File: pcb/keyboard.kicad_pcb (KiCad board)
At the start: 4 copper layers, 304.8 x 119.1 mm, 197 parts, among them J1 Conn_ARM_JTAG_SWD_10, J2 USB_C_Receptacle_USB2.0_16P, J3 Conn_Coaxial, K1 KEYSW, K10 KEYSW, K11 KEYSW, K12 KEYSW, K13 KEYSW, K14 KEYSW, K15 KEYSW, K16 KEYSW, K17 KEYSW, K18 KEYSW, K19 KEYSW, K2 KEYSW, K20 KEYSW, K21 KEYSW, K22 KEYSW, K23 KEYSW, K24 KEYSW, K25 KEYSW, K26 KEYSW, K27 KEYSW, K28 KEYSW, K29 KEYSW, K3 KEYSW, K30 KEYSW, K31 KEYSW, K32 KEYSW, K33 KEYSW, K34 KEYSW, K35 KEYSW, K36 KEYSW, K37 KEYSW, K38 KEYSW, K39 KEYSW, K4 KEYSW, K40 KEYSW, K41 KEYSW, K42 KEYSW, K43 KEYSW, K45 KEYSW, K46 KEYSW, K47 KEYSW, K48 KEYSW, K49 KEYSW, K5 KEYSW, K50 KEYSW, K51 KEYSW, K52 KEYSW, K53 KEYSW, K54 KEYSW, K55 KEYSW, K56 KEYSW, K57 KEYSW, K58 KEYSW, K59 KEYSW, K6 KEYSW, K60 KEYSW, K61 KEYSW, K62 KEYSW, K63 KEYSW, K67 KEYSW, K7 KEYSW, K70 KEYSW, K71 KEYSW, K72 KEYSW, K73 KEYSW, K74 KEYSW, K75 KEYSW, K8 KEYSW, K9 KEYSW, Q1 FDN340P, Q2 FS8025A, Q3 FDN340P, SW1 SW_SPST, SW2 SW_SPST, U1 nRF52840, U2 TP4056-42-ESOP8, U3 DW01A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

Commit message: Improve clock placement and round corners
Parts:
- moved C10 6.95 mm to (243.2, 86.3)
- moved C12 5.83 mm to (235.5, 81.0), turned to 90 degrees
- moved C2 3.64 mm to (242.0, 84.8), turned to 180 degrees
- moved L3 2.84 mm to (227.0, 80.0), turned to 180 degrees
- moved L2 2.09 mm to (227.0, 82.0), turned to 0 degrees
- moved X1 2.02 mm to (238.9, 83.0), turned to -45 degrees
- moved C1 1.81 mm to (237.0, 80.0)
- moved C13 1.35 mm to (234.0, 81.0)
- moved C16 1.11 mm to (231.0, 80.0)
- moved C15 1.09 mm to (231.0, 82.0)
- moved C9 0.22 mm to (239.8, 86.4)
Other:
- outline, holes or cut-outs redrawn

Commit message: Move some parts around lol
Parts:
- moved R3 83.9 mm to (115.0, 93.0), turned to 0 degrees
- moved F1 72.7 mm to (115.0, 87.0), turned to 90 degrees
- moved D64 61.1 mm to (107.0, 93.0), turned to 0 degrees
- moved C11 57.2 mm to (153.7, 94.0)
- moved Q2 52.4 mm to (151.0, 86.0)
- moved U3 51.2 mm to (141.0, 86.0)
- moved R6 45.5 mm to (137.0, 81.0), turned to 0 degrees
- moved D68 44.1 mm to (130.0, 84.0), turned to 90 degrees
- moved R8 40.9 mm to (133.0, 86.0), turned to 0 degrees
- moved R9 37.3 mm to (146.0, 86.0), turned to 0 degrees
- moved R11 28.5 mm to (132.0, 80.0), turned to -90 degrees
- moved C17 28.3 mm to (137.0, 85.0), turned to 90 degrees
- moved C18 24.3 mm to (141.0, 82.0), turned to -90 degrees
- moved Q1 21.7 mm to (119.0, 84.0)
- moved Q3 19.7 mm to (125.5, 84.0)
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
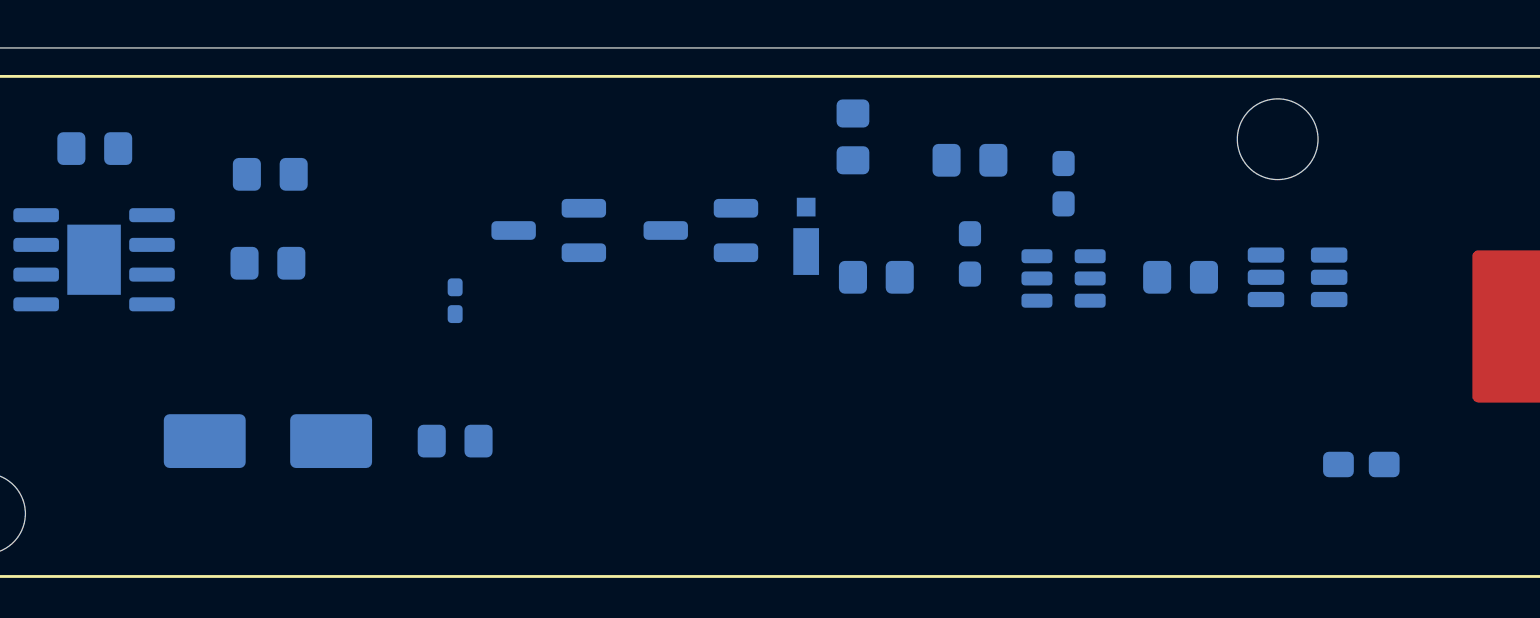
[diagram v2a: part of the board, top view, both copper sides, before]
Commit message: Finish initial placement
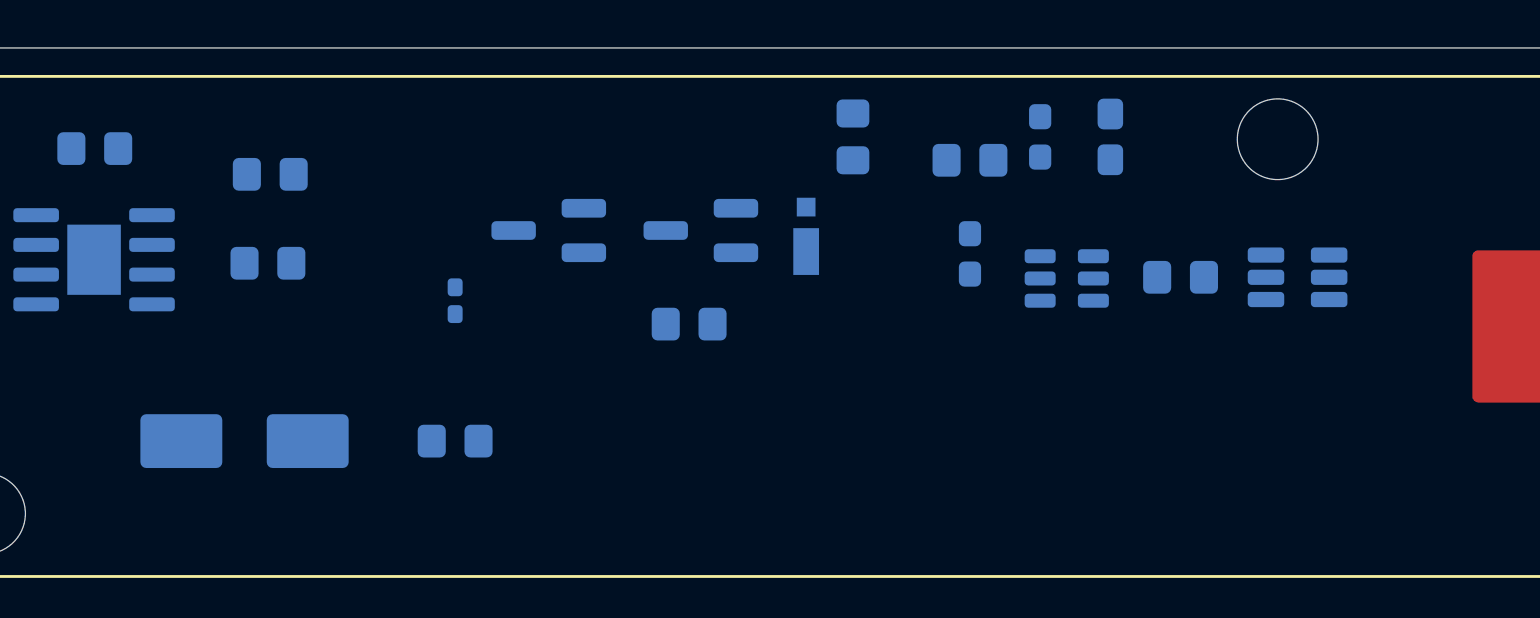
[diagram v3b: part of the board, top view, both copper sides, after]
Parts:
- moved C11 17.6 mm to (143.0, 80.0), turned to 90 degrees
- moved R8 8.25 mm to (125.0, 88.0)
- moved C18 2.24 mm to (140.0, 80.0), turned to 90 degrees
- moved D64 1.00 mm to (106.0, 93.0)
- moved U3 0.14 mm to (141.1, 86.0)
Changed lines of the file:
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@@
 		(tags "resistor handsolder")
 		(property "Reference" "R6"
-			(at 0 1.65 0)
+			(at 0 -1.6 0)
 			(layer "B.SilkS")
 			(effects
@@
 	(footprint "Diode_SMD:D_SMB_Handsoldering"
 		(layer "B.Cu")
-		(at 107 93)
+		(at 106 93)
 		(descr "Diode SMB (DO-214AA) Handsoldering")
 		(tags "Diode SMB (DO-214AA) Handsoldering")
@@
 	(footprint "Resistor_SMD:R_0805_2012Metric_Pad1.20x1.40mm_HandSolder"
 		(layer "B.Cu")
-		(at 133 86)
+		(at 125 88)
 		(descr "Resistor SMD 0805 (2012 Metric), square (rectangular) end terminal, IPC-7351 nominal with elongated pad for handsoldering. (Body size source: IPC-SM-782 page 72, https://www.pcb-3d.com/wordpress/wp-content/uploads/ipc-sm-782a_amendment_1_and_2.pdf)")
 		(tags "resistor handsolder")
@@
 	(footprint "Package_TO_SOT_SMD:SOT-23-6"
 		(layer "B.Cu")
-		(at 141 86.05 180)
+		(at 141.1375 86.05 180)
 		(descr "SOT, 6 Pin (JEDEC MO-178 Var AB https://www.jedec.org/document_search?search_api_views_fulltext=MO-178)")
 		(tags "SOT TO_SOT_SMD")
@@
 	(footprint "Capacitor_Tantalum_SMD:CP_EIA-2012-15_AVX-P_HandSolder"
 		(layer "B.Cu")
-		(at 153.725 94 180)
+		(at 143 80 90)
 		(descr "Tantalum Capacitor SMD AVX-P (2012-15 Metric), IPC-7352 nominal, (Body size from: https://www.vishay.com/docs/40182/tmch.pdf)")
 		(tags "capacitor tantalum")
 		(property "Reference" "C11"
-			(at 0 1.58 0)
+			(at 0 1.58 90)
 			(layer "B.SilkS")
 			(effects
@@
 		)
 		(property "Value" "10µF"
-			(at 0 -1.58 0)
+			(at 0 -1.58 90)
 			(layer "B.Fab")
 			(hide yes)
@@
 		)
 		(property "Datasheet" ""
-			(at 0 0 0)
+			(at 0 0 90)
 			(layer "B.Fab")
 			(hide yes)
@@
 		)
 		(property "Description" "Polarized capacitor"
-			(at 0 0 0)
+			(at 0 0 90)
 			(layer "B.Fab")
 			(hide yes)
@@
 		)
 		(property "KiLib_Generator" "SMD_2terminal_chip_molded"
-			(at 0 0 0)
+			(at 0 0 90)
 			(layer "B.SilkS")
 			(hide yes)
@@
 		(duplicate_pad_numbers_are_jumpers no)
 		(fp_line
-			(start 1 0.805)
-			(end -1.895 0.805)
+			(start -1.895 -0.805)
+			(end 1 -0.805)
 			(stroke
 				(width 0.12)
@@
 		)
 		(fp_line
-			(start -1.895 0.805)
-			(end -1.895 -0.805)
+			(start 1 0.805)
+			(end -1.895 0.805)
 			(stroke
 				(width 0.12)
@@
 		)
 		(fp_line
-			(start -1.895 -0.805)
-			(end 1 -0.805)
+			(start -1.895 0.805)
+			(end -1.895 -0.805)
 			(stroke
 				(width 0.12)
@@
 		)
 		(fp_line
-			(start 1 0.625)
-			(end -0.6875 0.625)
+			(start 1 -0.625)
+			(end 1 0.625)
 			(stroke
 				(width 0.1)
@@
 		)
 		(fp_line
-			(start 1 -0.625)
-			(end 1 0.625)
+			(start -1 -0.625)
+			(end 1 -0.625)
 			(stroke
 				(width 0.1)
@@
 		)
 		(fp_line
-			(start -0.6875 0.625)
-			(end -1 0.3125)
+			(start -1 0.3125)
+			(end -1 -0.625)
 			(stroke
 				(width 0.1)
@@
 		)
 		(fp_line
-			(start -1 0.3125)
-			(end -1 -0.625)
+			(start 1 0.625)
+			(end -0.6875 0.625)
 			(stroke
 				(width 0.1)
@@
 		)
 		(fp_line
-			(start -1 -0.625)
-			(end 1 -0.625)
+			(start -0.6875 0.625)
+			(end -1 0.3125)
 			(stroke
 				(width 0.1)
@@
 		)
 		(fp_text user "${REFERENCE}"
-			(at 0 0 0)
+			(at 0 0 90)
 			(layer "B.Fab")
 			(effects
@@
 		)
 		(pad "1" smd roundrect
-			(at -0.9775 0 180)
+			(at -0.9775 0 90)
 			(size 1.315 1.09)
 			(layers "B.Cu" "B.Mask" "B.Paste")
@@
 		)
 		(pad "2" smd roundrect
-			(at 0.9775 0 180)
+			(at 0.9775 0 90)
 			(size 1.315 1.09)
 			(layers "B.Cu" "B.Mask" "B.Paste")
@@
 	(footprint "Capacitor_SMD:C_0603_1608Metric_Pad1.08x0.95mm_HandSolder"
 		(layer "B.Cu")
-		(at 141 82 -90)
+		(at 140 80 90)
 		(descr "Capacitor SMD 0603 (1608 Metric), square (rectangular) end terminal, IPC-7351 nominal with elongated pad for handsoldering. (Body size source: IPC-SM-782 page 76, https://www.pcb-3d.com/wordpress/wp-content/uploads/ipc-sm-782a_amendment_1_and_2.pdf)")
 		(tags "capacitor handsolder")
@@
 		(duplicate_pad_numbers_are_jumpers no)
 		(fp_line
-			(start -0.146267 0.51)
-			(end 0.146267 0.51)
+			(start -0.146267 -0.51)
+			(end 0.146267 -0.51)
 			(stroke
 				(width 0.12)
@@
 		)
 		(fp_line
-			(start -0.146267 -0.51)
-			(end 0.146267 -0.51)
+			(start -0.146267 0.51)
+			(end 0.146267 0.51)
 			(stroke
 				(width 0.12)
@@
 		)
 		(pad "1" smd roundrect
-			(at -0.8625 0 270)
+			(at -0.8625 0 90)
 			(size 1.075 0.95)
 			(layers "B.Cu" "B.Mask" "B.Paste")
@@
 		)
 		(pad "2" smd roundrect
-			(at 0.8625 0 270)
+			(at 0.8625 0 90)
 			(size 1.075 0.95)
 			(layers "B.Cu" "B.Mask" "B.Paste")

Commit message: Add mounting points
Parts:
- added H1: MountingHole_Pad, MountingHole:MountingHole_2.2mm_M2_Pad_Via, F.Cu at (55.0, 85.0)
- added H2: MountingHole_Pad, MountingHole:MountingHole_2.2mm_M2_Pad_Via, F.Cu at (250.0, 81.2)
- added H3: MountingHole_Pad, MountingHole:MountingHole_2.2mm_M2_Pad_Via, F.Cu at (332.0, 121.0)
- added H4: MountingHole_Pad, MountingHole:MountingHole_2.2mm_M2_Pad_Via, F.Cu at (140.0, 186.0)
- added H5: MountingHole_Pad, MountingHole:MountingHole_2.2mm_M2_Pad_Via, F.Cu at (164.8, 81.0)
- added H6: MountingHole_Pad, MountingHole:MountingHole_2.2mm_M2_Pad_Via, F.Cu at (71.0, 184.0)
- added H7: MountingHole_Pad, MountingHole:MountingHole_2.2mm_M2_Pad_Via, F.Cu at (235.0, 184.8)
- added H8: MountingHole_Pad, MountingHole:MountingHole_2.2mm_M2_Pad_Via, F.Cu at (310.0, 175.0)
- added H9: MountingHole_Pad, MountingHole:MountingHole_2.2mm_M2_Pad_Via, F.Cu at (195.0, 139.0)

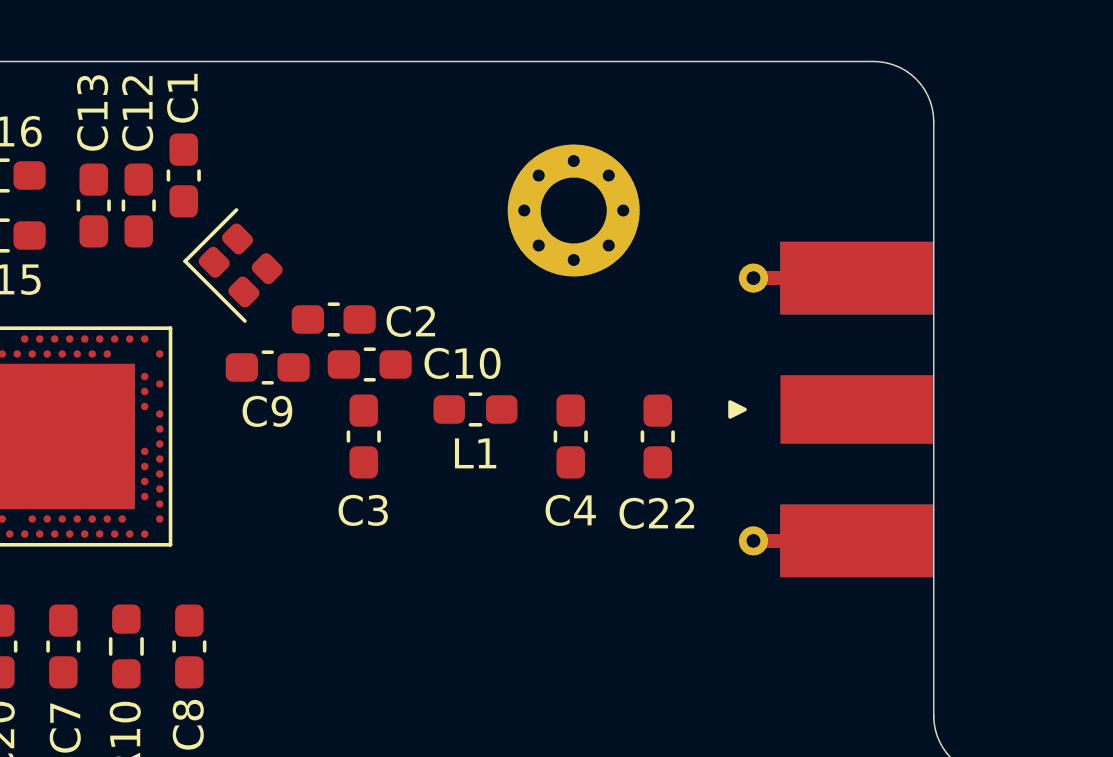
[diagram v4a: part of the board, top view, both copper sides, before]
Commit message: Add final hand solder footprints
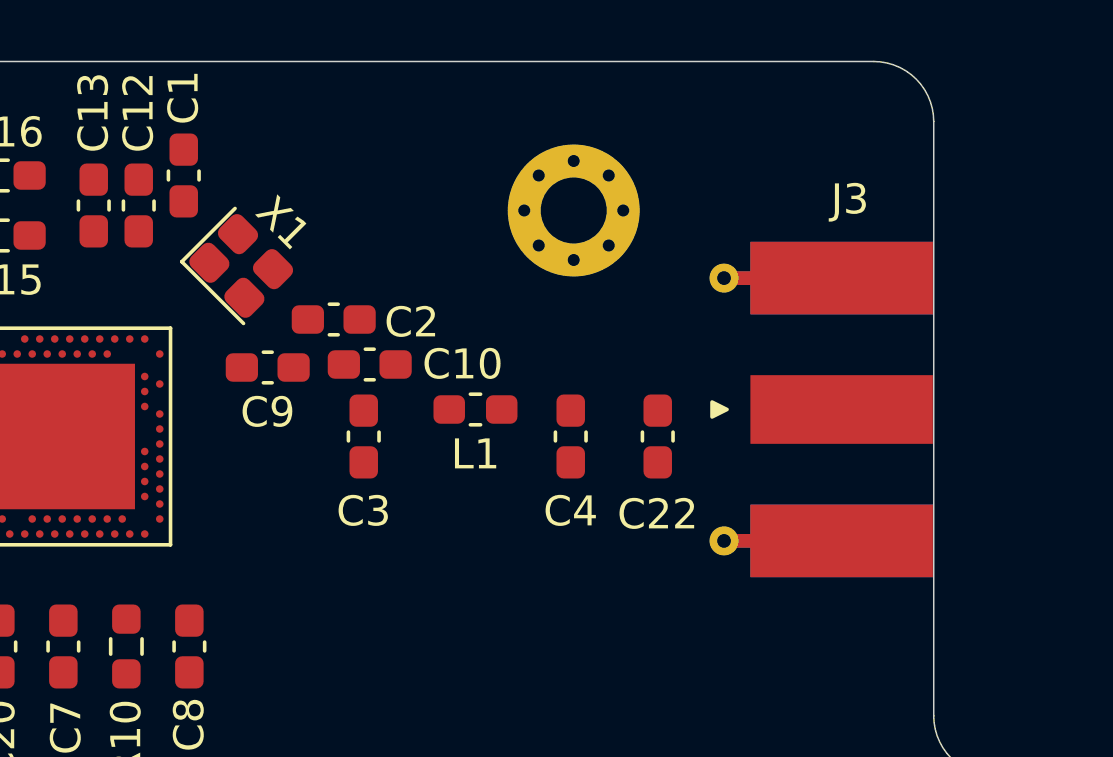
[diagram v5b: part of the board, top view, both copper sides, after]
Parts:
- J3: footprint Connector_Coaxial:SMA_Molex_73251-1153_EdgeMount_Horizontal -> My_Footprints:SMA_Molex_73251-1153_EdgeMount_Horizontal_HandSolder
- X1: footprint Crystal:Crystal_SMD_2016-4Pin_2.0x1.6mm -> My_Footprints:Crystal_SMD_2016-4Pin_2.0x1.6mm_HandSolder
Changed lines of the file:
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@@
 		(embedded_fonts no)
 	)
-	(footprint "Crystal:Crystal_SMD_2016-4Pin_2.0x1.6mm"
+	(footprint "My_Footprints:Crystal_SMD_2016-4Pin_2.0x1.6mm_HandSolder"
 		(layer "F.Cu")
 		(at 238.9 83 -45)
 		(descr "SMD2016/4, Crystal, 2.0x1.6mm package, SMD, http://www.q-crystal.com/upload/5/2015552223166229.pdf")
 		(property "Reference" "X1"
-			(at 0.000001 2.199999 135)
+			(at 0 -2.000001 315)
 			(layer "F.SilkS")
-			(hide yes)
 			(effects
 				(font
@@
 		)
 		(property "Value" "32MHz"
-			(at 0 2.000001 135)
+			(at 0 2.000001 315)
 			(layer "F.Fab")
 			(hide yes)
@@
 		)
 		(property "Datasheet" ""
-			(at 0 0 135)
+			(at 0 0 315)
 			(layer "F.Fab")
 			(hide yes)
@@
 		)
 		(property "Description" ""
-			(at 0 0 135)
+			(at 0 0 315)
 			(layer "F.Fab")
 			(hide yes)
@@
 		)
 		(property "KiLib_Generator" "crystal_resonator_oscillator"
-			(at 0 0 135)
+			(at 0 0 315)
 			(layer "F.SilkS")
 			(hide yes)
@@
 		(duplicate_pad_numbers_are_jumpers no)
 		(fp_line
-			(start -1.41 1.21)
-			(end 1.41 1.21)
+			(start -1.478319 1.3)
+			(end 1.431681 1.3)
 			(stroke
 				(width 0.12)
@@
 		)
 		(fp_line
-			(start -1.41 -1.21)
-			(end -1.41 1.21)
+			(start -1.478319 -1.21)
+			(end -1.478319 1.3)
 			(stroke
 				(width 0.12)
@@
 		(fp_poly
 			(pts
-				(xy -1.5 -1.3) (xy 1.5 -1.3) (xy 1.5 1.3) (xy -1.5 1.3)
+				(xy -1.578319 -1.3) (xy 1.521681 -1.3) (xy 1.52168 1.4) (xy -1.57832 1.4)
 			)
 			(stroke
@@
 		(fp_poly
 			(pts
-				(xy 1 -0.800001) (xy 1 0.8) (xy -0.6 0.799999) (xy -1 0.4) (xy -1 -0.8)
+				(xy 1.021681 -0.8) (xy 1.021681 0.8) (xy -0.578319 0.8) (xy -0.978319 0.4) (xy -0.978319 -0.799999)
 			)
 			(stroke
@@
 		)
 		(fp_text user "${REFERENCE}"
-			(at 0 0 135)
+			(at 0 0 315)
 			(layer "F.Fab")
 			(effects
@@
 		)
 		(pad "1" smd roundrect
-			(at -0.7 0.55 315)
-			(size 0.9 0.8)
+			(at -0.803319 0.675 315)
+			(size 1.15 1.05)
 			(layers "F.Cu" "F.Mask" "F.Paste")
 			(roundrect_rratio 0.25)
@@
 		)
 		(pad "2" smd roundrect
-			(at 0.7 0.55 315)
-			(size 0.9 0.8)
+			(at 0.846681 0.675 315)
+			(size 1.15 1.05)
 			(layers "F.Cu" "F.Mask" "F.Paste")
 			(roundrect_rratio 0.25)
@@
 		)
 		(pad "3" smd roundrect
-			(at 0.7 -0.55 315)
-			(size 0.9 0.8)
+			(at 0.846681 -0.675 315)
+			(size 1.15 1.05)
 			(layers "F.Cu" "F.Mask" "F.Paste")
 			(roundrect_rratio 0.25)
@@
 		)
 		(pad "4" smd roundrect
-			(at -0.7 -0.55 315)
-			(size 0.9 0.8)
+			(at -0.803319 -0.675 315)
+			(size 1.15 1.05)
 			(layers "F.Cu" "F.Mask" "F.Paste")
 			(roundrect_rratio 0.25)
@@
 		)
 	)
-	(footprint "Connector_Coaxial:SMA_Molex_73251-1153_EdgeMount_Horizontal"
+	(footprint "My_Footprints:SMA_Molex_73251-1153_EdgeMount_Horizontal_HandSolder"
 		(layer "F.Cu")
 		(at 257.71 87.8 180)
@@
 		(tags "sma edge")
 		(property "Reference" "J3"
-			(at -1.5 7 0)
+			(at -1.5 7 180)
 			(layer "F.SilkS")
-			(hide yes)
 			(effects
 				(font
@@
 		)
 		(property "Value" "Conn_Coaxial"
-			(at -1.72 -7.11 0)
+			(at -1.72 -7.11 180)
 			(layer "F.Fab")
+			(hide yes)
 			(effects
 				(font
@@
 		(fp_poly
 			(pts
-				(xy 2.5 -0.25) (xy 2 0) (xy 2.5 0.25)
+				(xy 3.1 -0.25) (xy 2.6 0) (xy 3.1 0.25)
 			)
 			(stroke
@@
 		)
 		(fp_line
-			(start 2.71 -6.09)
-			(end 2.71 6.09)
+			(start 4 -6.09)
+			(end 4 6.09)
 			(stroke
 				(width 0.05)
@@
 		(fp_line
 			(start -14.29 6.09)
-			(end 2.71 6.09)
+			(end 4 6.09)
 			(stroke
 				(width 0.05)
@@
 		(fp_line
 			(start -14.29 -6.09)
-			(end 2.71 -6.09)
+			(end 4 -6.09)
 			(stroke
 				(width 0.05)
@@
 		)
 		(fp_line
-			(start 2.71 -6.09)
-			(end 2.71 6.09)
+			(start 4 -6.09)
+			(end 4 6.09)
 			(stroke
 				(width 0.05)
@@
 		)
 		(fp_line
-			(start 2.71 -6.09)
+			(start 4 -6.09)
 			(end -14.29 -6.09)
 			(stroke
@@
 		(fp_line
 			(start -14.29 6.09)
-			(end 2.71 6.09)
+			(end 4 6.09)
 			(stroke
 				(width 0.05)
@@
 		(fp_poly
 			(pts
-				(xy 2.5 -0.251561) (xy 2 -0.001561) (xy 2.5 0.248439)
+				(xy 3.1 -0.251561) (xy 2.6 -0.001561) (xy 3.1 0.248439)
 			)
 			(stroke
@@
 		)
 		(fp_text user "${REFERENCE}"
-			(at -1.5 7 0)
+			(at -1.5 7 180)
 			(layer "F.Fab")
 			(effects
@@
 		)
 		(pad "1" smd rect
-			(at -1.72 0 180)
-			(size 5.08 2.29)
+			(at -1.22 0 180)
+			(size 6.08 2.29)
 			(layers "F.Cu" "F.Mask" "F.Paste")
 			(net "Net-(J3-In)")
@@
 		)
 		(pad "2" smd rect
-			(at -1.72 -4.38 180)
-			(size 5.08 2.42)
+			(at -1.22 -4.38 180)
+			(size 6.08 2.42)
 			(layers "F.Cu" "F.Mask" "F.Paste")
 			(net "GND")
@@
 		)
 		(pad "2" smd rect
-			(at -1.72 -4.38 180)
-			(size 5.08 2.42)
+			(at -1.22 -4.38 180)
+			(size 6.08 2.42)
 			(layers "B.Cu" "B.Mask" "B.Paste")
 			(net "GND")
@@
 		)
 		(pad "2" smd rect
-			(at -1.72 4.38 180)
-			(size 5.08 2.42)
+			(at -1.22 4.38 180)
+			(size 6.08 2.42)
 			(layers "F.Cu" "F.Mask" "F.Paste")
 			(net "GND")
@@
 		)
 		(pad "2" smd rect
-			(at -1.72 4.38 180)
-			(size 5.08 2.42)
+			(at -1.22 4.38 180)
+			(size 6.08 2.42)
 			(layers "B.Cu" "B.Mask" "B.Paste")
 			(net "GND")
@@
 		)
 		(pad "2" smd rect
-			(at 1.27 -4.38 180)
+			(at 2.25 -4.38 180)
 			(size 0.95 0.46)
 			(layers "F.Cu")
@@
 		)
 		(pad "2" smd rect
-			(at 1.27 -4.38 180)
+			(at 2.25 -4.38 180)
 			(size 0.95 0.46)
 			(layers "B.Cu")
@@
 		)
 		(pad "2" smd rect
-			(at 1.27 4.38 180)
+			(at 2.25 4.38 180)
 			(size 0.95 0.46)
 			(layers "F.Cu")
@@
 		)
 		(pad "2" smd rect
-			(at 1.27 4.38 180)
+			(at 2.25 4.38 180)
 			(size 0.95 0.46)
 			(layers "B.Cu")
@@
 		)
 		(pad "2" thru_hole circle
-			(at 1.72 -4.38 180)
+			(at 2.7 -4.38 180)
 			(size 0.97 0.97)
 			(drill 0.46)
@@
 		)
 		(pad "2" thru_hole circle
-			(at 1.72 4.38 180)
+			(at 2.7 4.38 180)
 			(size 0.97 0.97)
 			(drill 0.46)
